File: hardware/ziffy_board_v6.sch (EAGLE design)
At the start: 27 parts, among them IC1 74HC125, IC2 74HC125, IC3 74HC125, IC4 74HC125, IC5 74HC125, IC6 74HC125

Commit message: tweaked
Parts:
- C1, C2: value 1uF -> 0.1uF; device A_butts:CAPACITOR-CERAMIC025-024X044 -> A_butts:CAPACITOR-CERAMICC0603
- C3, C4, C5, C6: device A_butts:CAPACITOR-CERAMIC025-024X044 -> A_butts:CAPACITOR-CERAMICC0603
- C7: value 0.1uF -> 1uF
- C8: value 0.1uF -> 1uF; device A_butts:CAPACITOR-CERAMIC025-024X044 -> A_butts:CAPACITOR-CERAMICC0805
- R4: device A_butts:RESISTORPTH-AXIAL-6.35MM -> A_butts:RESISTORPTH-AXIAL-5.08MM
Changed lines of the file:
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@@
 <grid distance="100" unitdist="mil" unit="mil" style="lines" multiple="1" display="yes" altdistance="2" altunitdist="mil" altunit="mil"/>
 <layers>
-<layer number="1" name="Top" color="4" fill="1" visible="no" active="no"/>
-<layer number="16" name="Bottom" color="1" fill="1" visible="no" active="no"/>
-<layer number="17" name="Pads" color="2" fill="1" visible="no" active="no"/>
-<layer number="18" name="Vias" color="2" fill="1" visible="no" active="no"/>
-<layer number="19" name="Unrouted" color="6" fill="1" visible="no" active="no"/>
-<layer number="20" name="Dimension" color="15" fill="1" visible="no" active="no"/>
-<layer number="21" name="tPlace" color="7" fill="1" visible="no" active="no"/>
-<layer number="22" name="bPlace" color="7" fill="1" visible="no" active="no"/>
-<layer number="23" name="tOrigins" color="15" fill="1" visible="no" active="no"/>
-<layer number="24" name="bOrigins" color="15" fill="1" visible="no" active="no"/>
-<layer number="25" name="tNames" color="7" fill="1" visible="no" active="no"/>
-<layer number="26" name="bNames" color="7" fill="1" visible="no" active="no"/>
-<layer number="27" name="tValues" color="7" fill="1" visible="no" active="no"/>
-<layer number="28" name="bValues" color="7" fill="1" visible="no" active="no"/>
+<layer number="1" name="Top" color="4" fill="1" visible="yes" active="no"/>
+<layer number="16" name="Bottom" color="1" fill="1" visible="yes" active="no"/>
+<layer number="17" name="Pads" color="2" fill="1" visible="yes" active="no"/>
+<layer number="18" name="Vias" color="2" fill="1" visible="yes" active="no"/>
+<layer number="19" name="Unrouted" color="6" fill="1" visible="yes" active="no"/>
+<layer number="20" name="Dimension" color="15" fill="1" visible="yes" active="no"/>
+<layer number="21" name="tPlace" color="7" fill="1" visible="yes" active="no"/>
+<layer number="22" name="bPlace" color="7" fill="1" visible="yes" active="no"/>
+<layer number="23" name="tOrigins" color="15" fill="1" visible="yes" active="no"/>
+<layer number="24" name="bOrigins" color="15" fill="1" visible="yes" active="no"/>
+<layer number="25" name="tNames" color="7" fill="1" visible="yes" active="no"/>
+<layer number="26" name="bNames" color="7" fill="1" visible="yes" active="no"/>
+<layer number="27" name="tValues" color="7" fill="1" visible="yes" active="no"/>
+<layer number="28" name="bValues" color="7" fill="1" visible="yes" active="no"/>
 <layer number="29" name="tStop" color="7" fill="3" visible="no" active="no"/>
 <layer number="30" name="bStop" color="7" fill="6" visible="no" active="no"/>
@@
 <layer number="35" name="tGlue" color="7" fill="4" visible="no" active="no"/>
 <layer number="36" name="bGlue" color="7" fill="5" visible="no" active="no"/>
-<layer number="37" name="tTest" color="7" fill="1" visible="no" active="no"/>
-<layer number="38" name="bTest" color="7" fill="1" visible="no" active="no"/>
+<layer number="37" name="tTest" color="7" fill="1" visible="yes" active="no"/>
+<layer number="38" name="bTest" color="7" fill="1" visible="yes" active="no"/>
 <layer number="39" name="tKeepout" color="4" fill="11" visible="no" active="no"/>
 <layer number="40" name="bKeepout" color="1" fill="11" visible="no" active="no"/>
@@
 <layer number="44" name="Drills" color="7" fill="1" visible="no" active="no"/>
 <layer number="45" name="Holes" color="7" fill="1" visible="no" active="no"/>
-<layer number="46" name="Milling" color="3" fill="1" visible="no" active="no"/>
-<layer number="47" name="Measures" color="7" fill="1" visible="no" active="no"/>
-<layer number="48" name="Document" color="7" fill="1" visible="no" active="no"/>
-<layer number="49" name="Reference" color="7" fill="1" visible="no" active="no"/>
-<layer number="50" name="dxf" color="7" fill="1" visible="no" active="no"/>
-<layer number="51" name="tDocu" color="7" fill="1" visible="no" active="no"/>
-<layer number="52" name="bDocu" color="7" fill="1" visible="no" active="no"/>
-<layer number="53" name="tGND_GNDA" color="7" fill="9" visible="no" active="no"/>
-<layer number="54" name="bGND_GNDA" color="1" fill="9" visible="no" active="no"/>
-<layer number="56" name="wert" color="7" fill="1" visible="no" active="no"/>
-<layer number="57" name="tCAD" color="7" fill="1" visible="no" active="no"/>
+<layer number="46" name="Milling" color="3" fill="1" visible="yes" active="no"/>
+<layer number="47" name="Measures" color="7" fill="1" visible="yes" active="no"/>
+<layer number="48" name="Document" color="7" fill="1" visible="yes" active="no"/>
+<layer number="49" name="Reference" color="7" fill="1" visible="yes" active="no"/>
+<layer number="50" name="dxf" color="7" fill="1" visible="yes" active="no"/>
+<layer number="51" name="tDocu" color="7" fill="1" visible="yes" active="no"/>
+<layer number="52" name="bDocu" color="7" fill="1" visible="yes" active="no"/>
+<layer number="53" name="tGND_GNDA" color="7" fill="9" visible="yes" active="no"/>
+<layer number="54" name="bGND_GNDA" color="1" fill="9" visible="yes" active="no"/>
+<layer number="56" name="wert" color="7" fill="1" visible="yes" active="no"/>
+<layer number="57" name="tCAD" color="7" fill="1" visible="yes" active="no"/>
 <layer number="90" name="Modules" color="5" fill="1" visible="yes" active="yes"/>
 <layer number="91" name="Nets" color="2" fill="1" visible="yes" active="yes"/>
@@
 </classes>
 <parts>
-<part name="C1" library="A_butts" deviceset="CAPACITOR-CERAMIC" device="025-024X044" value="1uF"/>
+<part name="C1" library="A_butts" deviceset="CAPACITOR-CERAMIC" device="C0603" value="0.1uF"/>
 <part name="BUSY" library="A_butts" deviceset="LED" device="3MM" value="YELLOW"/>
 <part name="ERR" library="A_butts" deviceset="LED" device="3MM" value="RED"/>
 <part name="HI!" library="A_butts" deviceset="LED" device="3MM" value="GREEN"/>
-<part name="R4" library="A_butts" deviceset="RESISTOR" device="PTH-AXIAL-6.35MM" value="10k"/>
+<part name="R4" library="A_butts" deviceset="RESISTOR" device="PTH-AXIAL-5.08MM" value="10k"/>
 <part name="GND2" library="SparkFun-Aesthetics" deviceset="GND" device=""/>
 <part name="GND3" library="SparkFun-Aesthetics" deviceset="GND" device=""/>
 <part name="GND8" library="SparkFun-Aesthetics" deviceset="GND" device=""/>
-<part name="C2" library="A_butts" deviceset="CAPACITOR-CERAMIC" device="025-024X044" value="1uF"/>
+<part name="C2" library="A_butts" deviceset="CAPACITOR-CERAMIC" device="C0603" value="0.1uF"/>
 <part name="GND9" library="SparkFun-Aesthetics" deviceset="GND" device=""/>
 <part name="SUPPLY16" library="A_butts" deviceset="VCC" device=""/>
@@
 <part name="ISP" library="A_butts" deviceset="AVR_SPI_PRG_6" device="PTH-SHROUD" value="AVR_SPI_PRG_6PTH-SHROUD"/>
 <part name="!HOSTRST" library="A_butts" deviceset="M02" device="PTH"/>
-<part name="C3" library="A_butts" deviceset="CAPACITOR-CERAMIC" device="025-024X044" value="0.1uF"/>
+<part name="C3" library="A_butts" deviceset="CAPACITOR-CERAMIC" device="C0603" value="0.1uF"/>
 <part name="GND1" library="SparkFun-Aesthetics" deviceset="GND" device=""/>
 <part name="SUPPLY4" library="A_butts" deviceset="VCC" device=""/>
-<part name="C4" library="A_butts" deviceset="CAPACITOR-CERAMIC" device="025-024X044" value="0.1uF"/>
+<part name="C4" library="A_butts" deviceset="CAPACITOR-CERAMIC" device="C0603" value="0.1uF"/>
 <part name="GND4" library="SparkFun-Aesthetics" deviceset="GND" device=""/>
 <part name="SUPPLY7" library="A_butts" deviceset="VCC" device=""/>
@@
 <part name="SUPPLY12" library="A_butts" deviceset="VCC" device=""/>
 <part name="GND17" library="SparkFun-Aesthetics" deviceset="GND" device=""/>
-<part name="C5" library="A_butts" deviceset="CAPACITOR-CERAMIC" device="025-024X044" value="0.1uF"/>
+<part name="C5" library="A_butts" deviceset="CAPACITOR-CERAMIC" device="C0603" value="0.1uF"/>
 <part name="GND18" library="SparkFun-Aesthetics" deviceset="GND" device=""/>
 <part name="SUPPLY13" library="A_butts" deviceset="VCC" device=""/>
-<part name="C6" library="A_butts" deviceset="CAPACITOR-CERAMIC" device="025-024X044" value="0.1uF"/>
+<part name="C6" library="A_butts" deviceset="CAPACITOR-CERAMIC" device="C0603" value="0.1uF"/>
 <part name="GND19" library="SparkFun-Aesthetics" deviceset="GND" device=""/>
 <part name="SUPPLY14" library="A_butts" deviceset="VCC" device=""/>
-<part name="C7" library="A_butts" deviceset="CAPACITOR-CERAMIC" device="025-024X044" value="0.1uF"/>
+<part name="C7" library="A_butts" deviceset="CAPACITOR-CERAMIC" device="025-024X044" value="1uF"/>
 <part name="GND20" library="SparkFun-Aesthetics" deviceset="GND" device=""/>
 <part name="SUPPLY15" library="A_butts" deviceset="VCC" device=""/>
-<part name="C8" library="A_butts" deviceset="CAPACITOR-CERAMIC" device="025-024X044" value="0.1uF"/>
+<part name="C8" library="A_butts" deviceset="CAPACITOR-CERAMIC" device="C0805" value="1uF"/>
 <part name="GND21" library="SparkFun-Aesthetics" deviceset="GND" device=""/>
 <part name="SUPPLY18" library="A_butts" deviceset="VCC" device=""/>

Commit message: more twaddling
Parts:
- BUSY, ERR, HI!: device A_butts:LED3MM -> A_butts:LED1206
- R1, R2, R3: device A_butts:RESISTORPTH-AXIAL-6.35MM -> A_butts:RESISTORR0805
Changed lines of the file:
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@@
 <parts>
 <part name="C1" library="A_butts" deviceset="CAPACITOR-CERAMIC" device="C0603" value="0.1uF"/>
-<part name="BUSY" library="A_butts" deviceset="LED" device="3MM" value="YELLOW"/>
-<part name="ERR" library="A_butts" deviceset="LED" device="3MM" value="RED"/>
-<part name="HI!" library="A_butts" deviceset="LED" device="3MM" value="GREEN"/>
+<part name="BUSY" library="A_butts" deviceset="LED" device="1206" value="YELLOW"/>
+<part name="ERR" library="A_butts" deviceset="LED" device="1206" value="RED"/>
+<part name="HI!" library="A_butts" deviceset="LED" device="1206" value="GREEN"/>
 <part name="R4" library="A_butts" deviceset="RESISTOR" device="PTH-AXIAL-5.08MM" value="10k"/>
 <part name="GND2" library="SparkFun-Aesthetics" deviceset="GND" device=""/>
@@
 <part name="GND4" library="SparkFun-Aesthetics" deviceset="GND" device=""/>
 <part name="SUPPLY7" library="A_butts" deviceset="VCC" device=""/>
-<part name="R1" library="A_butts" deviceset="RESISTOR" device="PTH-AXIAL-6.35MM" value="330R"/>
-<part name="R2" library="A_butts" deviceset="RESISTOR" device="PTH-AXIAL-6.35MM" value="330R"/>
-<part name="R3" library="A_butts" deviceset="RESISTOR" device="PTH-AXIAL-6.35MM" value="330R"/>
+<part name="R1" library="A_butts" deviceset="RESISTOR" device="R0805" value="330R"/>
+<part name="R2" library="A_butts" deviceset="RESISTOR" device="R0805" value="330R"/>
+<part name="R3" library="A_butts" deviceset="RESISTOR" device="R0805" value="330R"/>
 <part name="TARGET_RESET" library="A_butts" deviceset="SPST-NO-TACT" device="6MM-PTH-SMALL-PADS" value="SPST-NO-TACT6MM-PTH-SMALL-PADS"/>
 <part name="GND12" library="SparkFun-Aesthetics" deviceset="GND" device=""/>

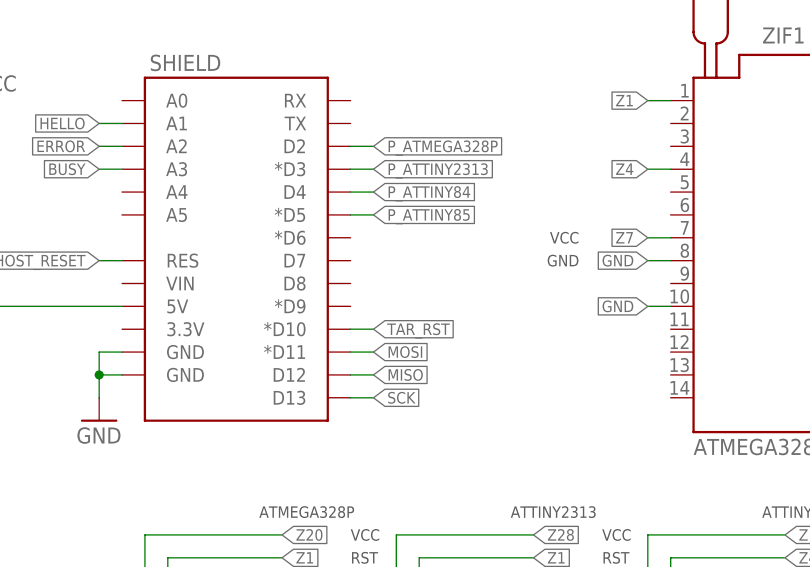
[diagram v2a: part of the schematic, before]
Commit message: routing done! mostly. now trying to return to pin-compat with original code base
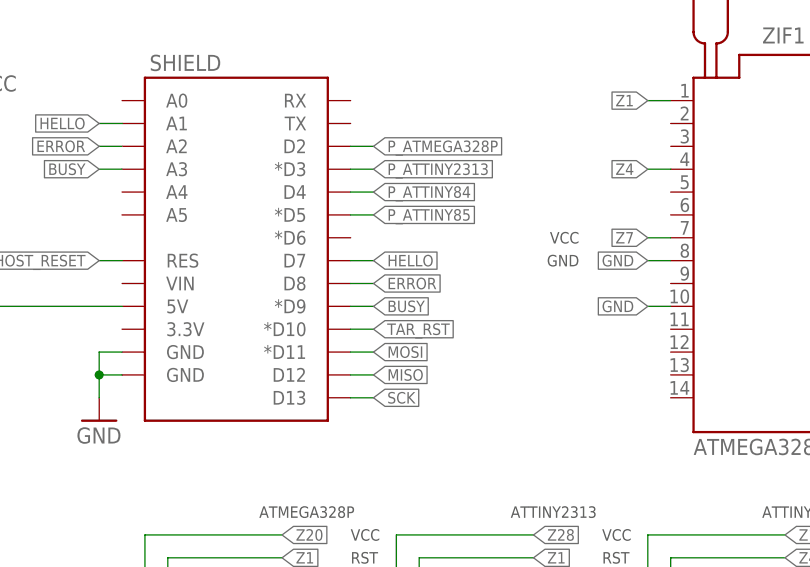
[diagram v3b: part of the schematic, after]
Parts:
- BUSY, ERR, HI!: device A_butts:LED1206 -> A_butts:LED3MM
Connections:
- net BUSY: now also SHIELD.*D9
- net ERROR: now also SHIELD.D8
- net HELLO: now also SHIELD.D7
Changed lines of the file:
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@@
 <parts>
 <part name="C1" library="A_butts" deviceset="CAPACITOR-CERAMIC" device="C0603" value="0.1uF"/>
-<part name="BUSY" library="A_butts" deviceset="LED" device="1206" value="YELLOW"/>
-<part name="ERR" library="A_butts" deviceset="LED" device="1206" value="RED"/>
-<part name="HI!" library="A_butts" deviceset="LED" device="1206" value="GREEN"/>
+<part name="BUSY" library="A_butts" deviceset="LED" device="3MM" value="YELLOW"/>
+<part name="ERR" library="A_butts" deviceset="LED" device="3MM" value="RED"/>
+<part name="HI!" library="A_butts" deviceset="LED" device="3MM" value="GREEN"/>
 <part name="R4" library="A_butts" deviceset="RESISTOR" device="PTH-AXIAL-5.08MM" value="10k"/>
 <part name="GND2" library="SparkFun-Aesthetics" deviceset="GND" device=""/>
@@
 <label x="83.82" y="137.16" size="1.27" layer="95" rot="R180" xref="yes"/>
 </segment>
+<segment>
+<pinref part="SHIELD" gate="G$1" pin="D7"/>
+<wire x1="111.76" y1="121.92" x2="114.3" y2="121.92" width="0.1524" layer="91"/>
+<label x="114.3" y="121.92" size="1.27" layer="95" xref="yes"/>
+</segment>
 </net>
 <net name="ERROR" class="0">
@@
 <label x="83.82" y="134.62" size="1.27" layer="95" rot="R180" xref="yes"/>
 </segment>
+<segment>
+<pinref part="SHIELD" gate="G$1" pin="D8"/>
+<wire x1="111.76" y1="119.38" x2="114.3" y2="119.38" width="0.1524" layer="91"/>
+<label x="114.3" y="119.38" size="1.27" layer="95" xref="yes"/>
+</segment>
 </net>
 <net name="BUSY" class="0">
@@
 <label x="83.82" y="132.08" size="1.27" layer="95" rot="R180" xref="yes"/>
 </segment>
-</net>
+<segment>
+<pinref part="SHIELD" gate="G$1" pin="*D9"/>
+<wire x1="111.76" y1="116.84" x2="114.3" y2="116.84" width="0.1524" layer="91"/>
+<label x="114.3" y="116.84" size="1.27" layer="95" xref="yes"/>
+</segment>
+</net>

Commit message: layout complete. replaced most of the surface mount caps w/PTH ones. still debating resistors for LEDs.
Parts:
- removed C8: 1uF, A_butts:CAPACITOR-CERAMICC0805
- C1, C2, C3, C4, C6: device A_butts:CAPACITOR-CERAMICC0603 -> A_butts:CAPACITOR-CERAMIC025-024X044
- C5: value 0.1uF -> 1uF; device A_butts:CAPACITOR-CERAMICC0603 -> A_butts:CAPACITOR-CERAMIC025-024X044
- SHIELD: value (none) -> YOUR MOTHER
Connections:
- net BUSY: no longer SHIELD.A3
- net ERROR: no longer SHIELD.A2
- net GND: no longer C8.2
- net HELLO: no longer SHIELD.A1
- net VCC: no longer C8.1
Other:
- note removed: "ATMEGA328P"
- note removed: "ATTINY2313"
- note removed: "ATTINY84"
- note removed: "ATTINY85"
- note removed: "MISO"
- note removed: "MOSI"
- note removed: "RST"
- note removed: "SCK"
- moved on the sheet: BUSY, C1, C2, C3, C4, C5, C6, C7, ERR, HI!, HOST_RESET, IC1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

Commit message: trying all the angles (ba-dum-tish)
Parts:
- R1, R2, R3: device A_butts:RESISTORR0805 -> A_butts:RESISTORPTH-AXIAL-5.08MM
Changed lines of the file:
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@@
 <part name="GND4" library="SparkFun-Aesthetics" deviceset="GND" device=""/>
 <part name="SUPPLY7" library="A_butts" deviceset="VCC" device=""/>
-<part name="R1" library="A_butts" deviceset="RESISTOR" device="R0805" value="330R"/>
-<part name="R2" library="A_butts" deviceset="RESISTOR" device="R0805" value="330R"/>
-<part name="R3" library="A_butts" deviceset="RESISTOR" device="R0805" value="330R"/>
+<part name="R1" library="A_butts" deviceset="RESISTOR" device="PTH-AXIAL-5.08MM" value="330R"/>
+<part name="R2" library="A_butts" deviceset="RESISTOR" device="PTH-AXIAL-5.08MM" value="330R"/>
+<part name="R3" library="A_butts" deviceset="RESISTOR" device="PTH-AXIAL-5.08MM" value="330R"/>
 <part name="TARGET_RESET" library="A_butts" deviceset="SPST-NO-TACT" device="6MM-PTH-SMALL-PADS" value="SPST-NO-TACT6MM-PTH-SMALL-PADS"/>
 <part name="GND12" library="SparkFun-Aesthetics" deviceset="GND" device=""/>
